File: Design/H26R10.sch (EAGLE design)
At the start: 66 parts, among them P1 HEXABIT_17.32_X2_NO_P5_P10_P1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, U1 STM32F091CBU6, U2 AD8275BRMZ, U3 ADR431ARMZ, U4 AD8295BCPZ-WP, U5 AD7687BRMZ, X1 XTALL_CSTCE8M00G52, X2 1751251, X3 CON-PHOENIX-350_1751277

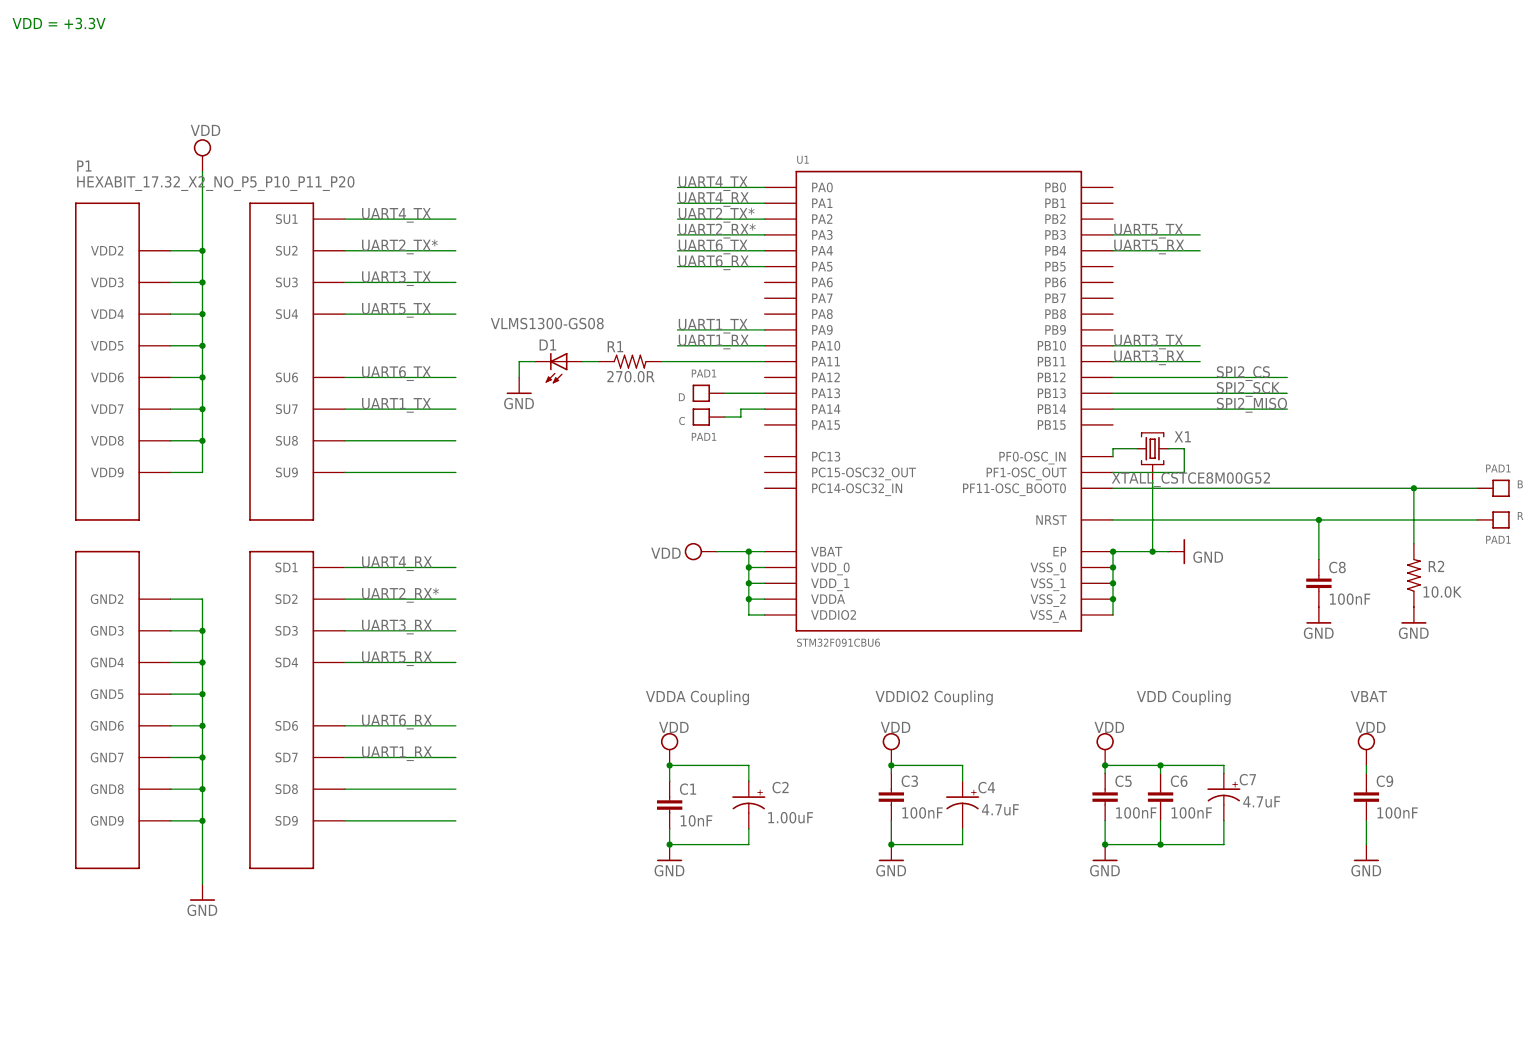
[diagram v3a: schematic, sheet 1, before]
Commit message: Replace MCU with Add STM32F091RB (LQFP64) and connect UARTs
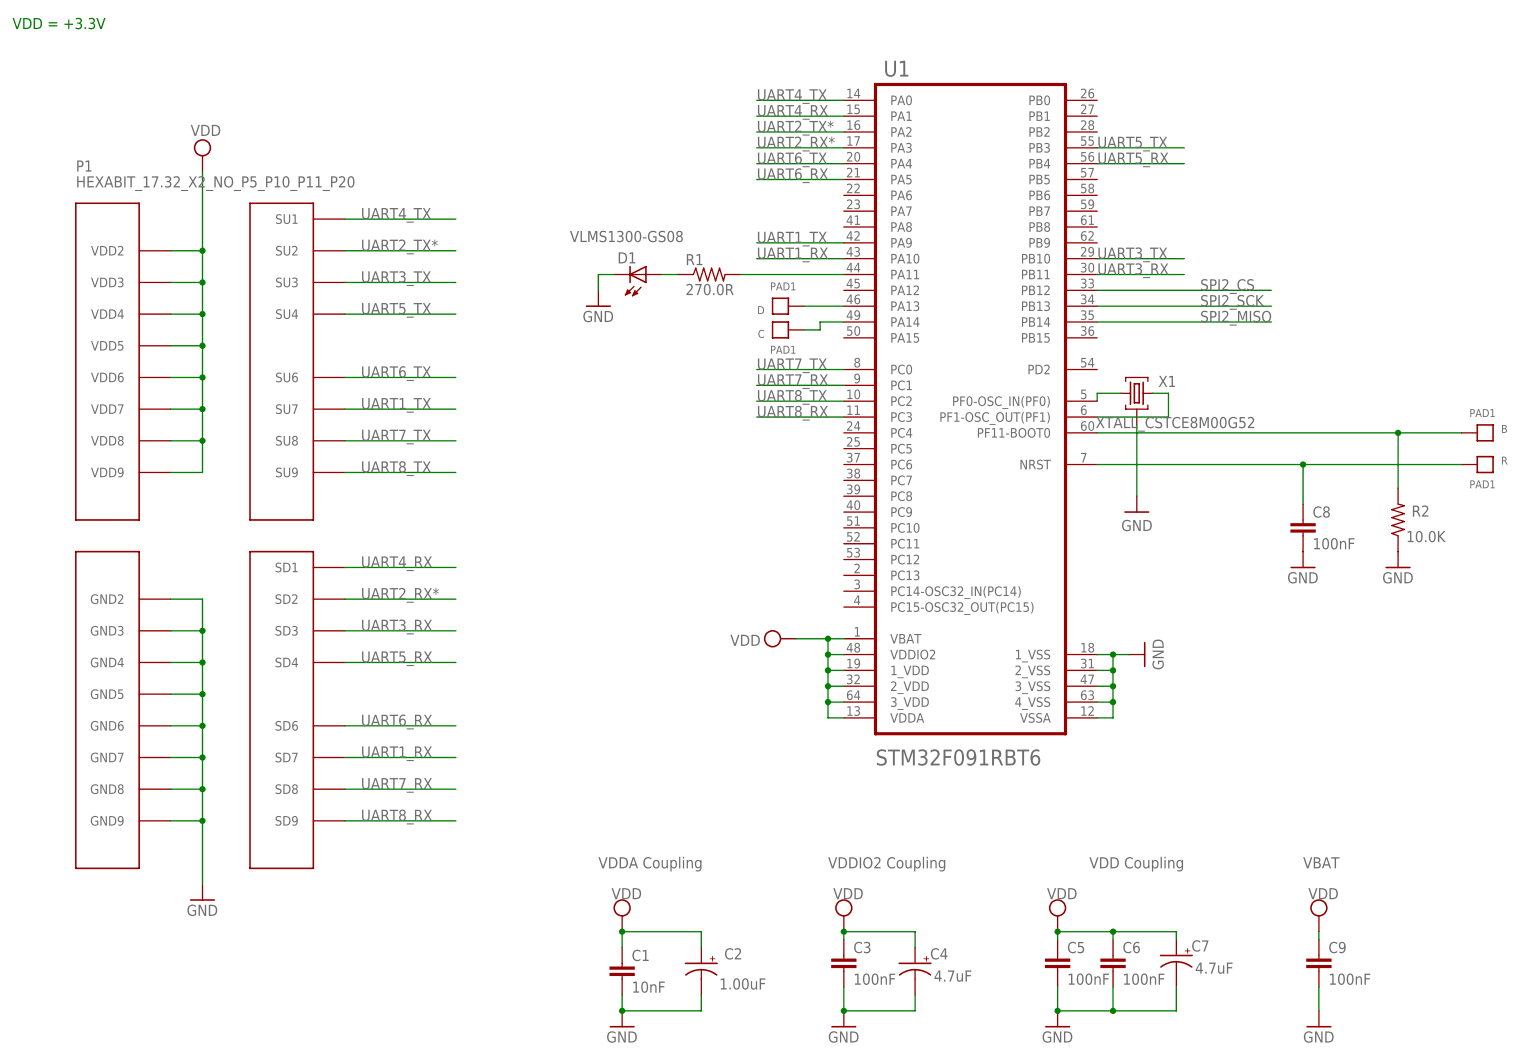
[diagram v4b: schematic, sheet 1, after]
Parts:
- U1: value STM32F091CBU6 -> STM32F091RBT6STMICROELECTRONICS_STM32F091RBT6_0_1; device Hexabitz:STM32F091CBU6 -> Hexabitz:STM32F091RBT6STMICROELECTRONICS_STM32F091RBT6_0_1
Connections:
- new net UART7_RX: U1.PC1
- new net UART7_TX: U1.PC0
- new net UART8_RX: U1.PC3
- new net UART8_TX: U1.PC2
- net B1: now also U1.PF11-BOOT0; no longer U1.PF11-OSC_BOOT0
- net GND: now also U1.1_VSS, U1.2_VSS, U1.3_VSS, U1.4_VSS, U1.VSSA; no longer U1.EP, U1.VSS_0, U1.VSS_1, U1.VSS_2, U1.VSS_A
- net N$5: now also U1.PF0-OSC_IN(PF0); no longer U1.PF0-OSC_IN
- net N$6: now also U1.PF1-OSC_OUT(PF1); no longer U1.PF1-OSC_OUT
- net VDD: now also U1.1_VDD, U1.2_VDD, U1.3_VDD; no longer U1.VDD_0, U1.VDD_1
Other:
- moved on the sheet: B, C, C1, C2, C3, C4, C5, C6, C7, C8, C9, D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

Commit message: Rearrange uart connections Route analog section
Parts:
- R3, R4, R6, R7, R8: device Hexabitz:R-0805 -> Hexabitz:R-0603
- renumbered X2 to PWR, X3 to AIN
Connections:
- net +5V renamed +2.5V
- removed net N$29: P1.SU1
- removed net N$30: P1.SU2
- removed net N$34: P1.SD1, P1.SD2, P1.SD3, P1.SD4, P1.SD6, P1.SD7, P1.SD8, P1.SD9, P1.SU3, P1.SU4, P1.SU6, P1.SU7, P1.SU8, P1.SU9
- removed net UART1_RX: U1.PA10
- removed net UART1_TX: U1.PA9
- new net UART1_RX*: P1.SD7, U1.PA10
- new net UART1_TX*: P1.SU7, U1.PA9
- net UART2_RX*: now also P1.SD3
- net UART2_TX*: now also P1.SU3
- net UART3_RX: now also P1.SD6
- net UART3_TX: now also P1.SU6
- net UART4_RX: now also P1.SD2
- net UART4_TX: now also P1.SU2
- net UART5_RX: now also P1.SD8
- net UART5_TX: now also P1.SU8
- net UART6_RX: now also P1.SD4
- net UART6_TX: now also P1.SU4
- net UART7_RX: now also P1.SD9
- net UART7_TX: now also P1.SU9
- net UART8_RX: now also P1.SD1
- net UART8_TX: now also P1.SU1

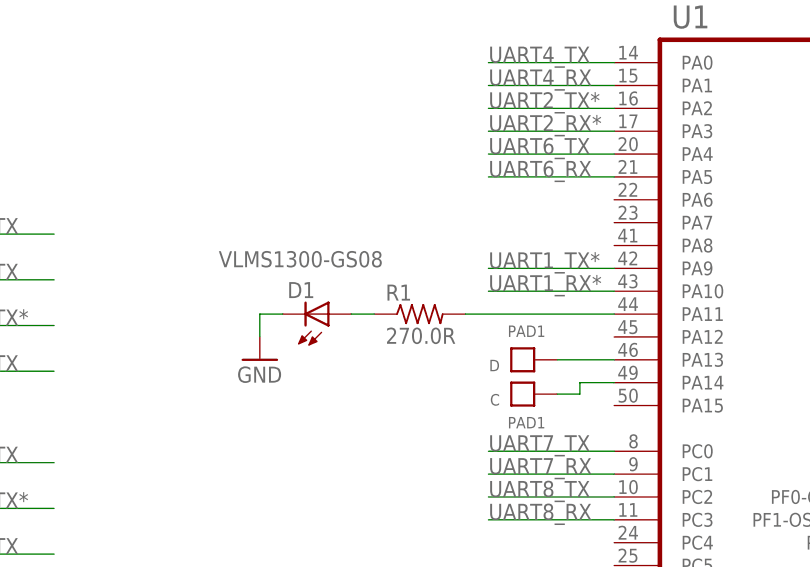
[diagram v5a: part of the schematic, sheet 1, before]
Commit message: More routing Add 2 more layers Add layer stack note
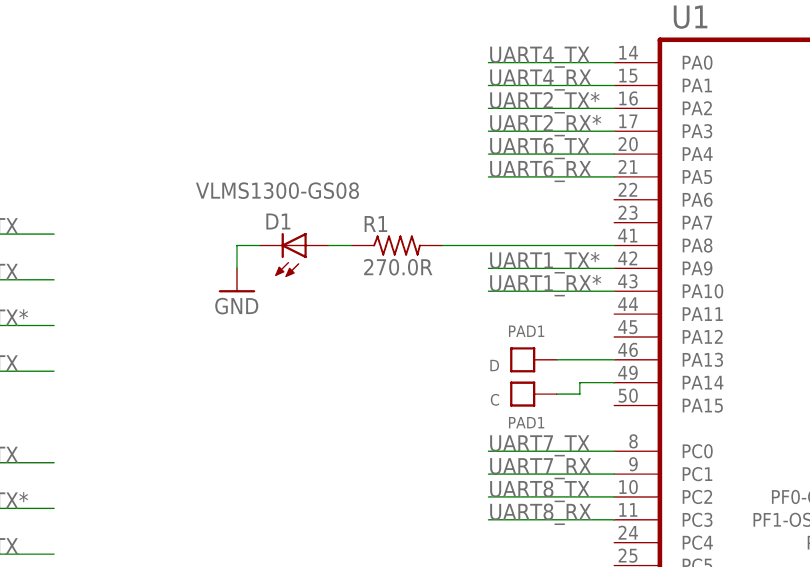
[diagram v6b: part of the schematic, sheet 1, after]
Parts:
- R5: device Hexabitz:R-0805 -> Hexabitz:R-0603
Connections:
- net N$3: now also U1.PA8; no longer U1.PA11
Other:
- moved on the sheet: D1, R1
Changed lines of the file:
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@@
 <setting verticaltext="up"/>
 </settings>
-<grid distance="50" unitdist="mil" unit="mil" style="lines" multiple="1" display="no" altdistance="0.01" altunitdist="inch" altunit="inch"/>
+<grid distance="0.1" unitdist="inch" unit="inch" style="lines" multiple="1" display="no" altdistance="0.01" altunitdist="inch" altunit="inch"/>
 <layers>
 <layer number="1" name="Top" color="4" fill="1" visible="no" active="no"/>
@@
 <part name="SUPPLY3" library="supply2" deviceset="VDD" device=""/>
 <part name="SUPPLY16" library="supply2" library_urn="urn:adsk.eagle:library:372" deviceset="+5V" device="" value="A2V5"/>
-<part name="R5" library="Hexabitz" deviceset="R-0805" device="" value="1.00K">
+<part name="R5" library="Hexabitz" deviceset="R-0603" device="" value="1.00K">
 <attribute name="MFN" value="Yageo"/>
 <attribute name="MPN" value="RC0603FR-0710KL"/>
@@
 <attribute name="VALUE" x="136.144" y="49.149" size="1.778" layer="96" rot="MR0"/>
 </instance>
-<instance part="R1" gate="G$1" x="127" y="163.83" smashed="yes">
-<attribute name="NAME" x="123.19" y="165.3286" size="1.778" layer="95"/>
-<attribute name="VALUE" x="123.19" y="160.528" size="1.778" layer="96"/>
-</instance>
-<instance part="D1" gate="G$1" x="116.84" y="163.83" smashed="yes" rot="MR180">
-<attribute name="NAME" x="112.268" y="167.386" size="1.778" layer="95" rot="MR180"/>
-<attribute name="VALUE" x="104.648" y="170.815" size="1.778" layer="96" rot="MR180"/>
+<instance part="R1" gate="G$1" x="124.46" y="171.45" smashed="yes">
+<attribute name="NAME" x="120.65" y="172.9486" size="1.778" layer="95"/>
+<attribute name="VALUE" x="120.65" y="168.148" size="1.778" layer="96"/>
+</instance>
+<instance part="D1" gate="G$1" x="114.3" y="171.45" smashed="yes" rot="MR180">
+<attribute name="NAME" x="109.728" y="175.006" size="1.778" layer="95" rot="MR180"/>
+<attribute name="VALUE" x="102.108" y="178.435" size="1.778" layer="96" rot="MR180"/>
 </instance>
 <instance part="X1" gate="G$1" x="195.58" y="144.78" smashed="yes">
@@
 <attribute name="VALUE" x="214.63" y="140.97" size="1.778" layer="96" rot="R180"/>
 </instance>
-<instance part="GND1" gate="1" x="109.22" y="158.75" smashed="yes">
-<attribute name="VALUE" x="106.68" y="156.21" size="1.778" layer="96"/>
+<instance part="GND1" gate="1" x="106.68" y="166.37" smashed="yes">
+<attribute name="VALUE" x="104.14" y="163.83" size="1.778" layer="96"/>
 </instance>
 <instance part="SUPPLY4" gate="G$1" x="138.43" y="105.41" smashed="yes" rot="R90">
@@
 <segment>
 <pinref part="GND1" gate="1" pin="GND"/>
-<wire x1="109.22" y1="161.29" x2="109.22" y2="163.83" width="0.1524" layer="91"/>
+<wire x1="106.68" y1="168.91" x2="106.68" y2="171.45" width="0.1524" layer="91"/>
 <pinref part="D1" gate="G$1" pin="C"/>
-<wire x1="109.22" y1="163.83" x2="111.76" y2="163.83" width="0.1524" layer="91"/>
+<wire x1="106.68" y1="171.45" x2="109.22" y2="171.45" width="0.1524" layer="91"/>
 </segment>
 <segment>
@@
 </segment>
 </net>
-<net name="N$3" class="0">
-<segment>
-<pinref part="R1" gate="G$1" pin="2"/>
-<wire x1="148.59" y1="163.83" x2="132.08" y2="163.83" width="0.1524" layer="91"/>
-<pinref part="U1" gate="G$0" pin="PA11"/>
-</segment>
-</net>
 <net name="N$4" class="0">
 <segment>
 <pinref part="R1" gate="G$1" pin="1"/>
 <pinref part="D1" gate="G$1" pin="A"/>
-<wire x1="121.92" y1="163.83" x2="119.38" y2="163.83" width="0.1524" layer="91"/>
+<wire x1="119.38" y1="171.45" x2="116.84" y2="171.45" width="0.1524" layer="91"/>
 </segment>
 </net>
@@
 </segment>
 </net>
+<net name="N$3" class="0">
+<segment>
+<pinref part="R1" gate="G$1" pin="2"/>
+<pinref part="U1" gate="G$0" pin="PA8"/>
+<wire x1="129.54" y1="171.45" x2="148.59" y2="171.45" width="0.1524" layer="91"/>
+</segment>
+</net>

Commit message: Finished routing Added polygons
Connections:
- removed net N$24: C13.2, C14.1, FB2.2
- net AGND: now also C11.GND, C12.GND, C13.2, C14.1, FB2.2
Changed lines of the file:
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@@
 <setting verticaltext="up"/>
 </settings>
-<grid distance="0.1" unitdist="inch" unit="inch" style="lines" multiple="1" display="no" altdistance="0.01" altunitdist="inch" altunit="inch"/>
+<grid distance="50" unitdist="mil" unit="mil" style="lines" multiple="1" display="no" altdistance="0.01" altunitdist="inch" altunit="inch"/>
 <layers>
 <layer number="1" name="Top" color="4" fill="1" visible="no" active="no"/>
@@
 </part>
 <part name="SUPPLY22" library="supply2" library_urn="urn:adsk.eagle:library:372" deviceset="AGND" device=""/>
-<part name="SUPPLY19" library="supply2" library_urn="urn:adsk.eagle:library:372" deviceset="AGND" device=""/>
 <part name="SUPPLY28" library="supply2" library_urn="urn:adsk.eagle:library:372" deviceset="AGND" device=""/>
 <part name="SUPPLY27" library="supply2" library_urn="urn:adsk.eagle:library:372" deviceset="+5V" device="" value="A2V5"/>
@@
 <attribute name="VALUE" x="157.353" y="32.385" size="1.778" layer="96"/>
 </instance>
-<instance part="SUPPLY19" gate="G$1" x="149.86" y="35.56" smashed="yes">
-<attribute name="VALUE" x="147.193" y="32.385" size="1.778" layer="96"/>
-</instance>
 <instance part="SUPPLY28" gate="G$1" x="210.82" y="35.56" smashed="yes">
 <attribute name="VALUE" x="208.153" y="32.385" size="1.778" layer="96"/>
@@
 </segment>
 <segment>
+<pinref part="C18" gate="G$1" pin="2"/>
+<pinref part="FB2" gate="G$1" pin="2"/>
+<wire x1="149.86" y1="39.37" x2="149.86" y2="41.91" width="0.1524" layer="91"/>
+<wire x1="109.22" y1="39.37" x2="121.92" y2="39.37" width="0.1524" layer="91"/>
+<pinref part="C13" gate="G$1" pin="2"/>
+<wire x1="121.92" y1="39.37" x2="138.43" y2="39.37" width="0.1524" layer="91"/>
+<wire x1="138.43" y1="41.91" x2="138.43" y2="39.37" width="0.1524" layer="91"/>
+<junction x="138.43" y="39.37"/>
+<pinref part="C14" gate="G$1" pin="1"/>
+<wire x1="138.43" y1="39.37" x2="138.43" y2="36.83" width="0.1524" layer="91"/>
+<pinref part="C11" gate="G$0" pin="GND"/>
+<wire x1="121.92" y1="43.18" x2="121.92" y2="39.37" width="0.1524" layer="91"/>
+<junction x="121.92" y="39.37"/>
+<pinref part="C12" gate="G$0" pin="GND"/>
+<wire x1="121.92" y1="39.37" x2="121.92" y2="35.56" width="0.1524" layer="91"/>
+<wire x1="138.43" y1="39.37" x2="149.86" y2="39.37" width="0.1524" layer="91"/>
+<junction x="149.86" y="39.37"/>
 <pinref part="C19" gate="G$1" pin="2"/>
 <pinref part="SUPPLY22" gate="G$1" pin="AGND"/>
-<wire x1="160.02" y1="38.1" x2="160.02" y2="41.91" width="0.1524" layer="91"/>
-</segment>
-<segment>
-<pinref part="C18" gate="G$1" pin="2"/>
-<pinref part="SUPPLY19" gate="G$1" pin="AGND"/>
-<wire x1="149.86" y1="38.1" x2="149.86" y2="41.91" width="0.1524" layer="91"/>
+<wire x1="160.02" y1="38.1" x2="160.02" y2="39.37" width="0.1524" layer="91"/>
+<wire x1="160.02" y1="39.37" x2="160.02" y2="41.91" width="0.1524" layer="91"/>
+<wire x1="149.86" y1="39.37" x2="160.02" y2="39.37" width="0.1524" layer="91"/>
+<junction x="160.02" y="39.37"/>
 </segment>
 <segment>
@@
 </segment>
 </net>
-<net name="N$24" class="0">
-<segment>
-<pinref part="FB2" gate="G$1" pin="2"/>
-<wire x1="109.22" y1="39.37" x2="121.92" y2="39.37" width="0.1524" layer="91"/>
-<wire x1="121.92" y1="39.37" x2="138.43" y2="39.37" width="0.1524" layer="91"/>
-<wire x1="121.92" y1="45.72" x2="121.92" y2="39.37" width="0.1524" layer="91"/>
-<junction x="121.92" y="39.37"/>
-<wire x1="121.92" y1="33.02" x2="121.92" y2="39.37" width="0.1524" layer="91"/>
-<pinref part="C13" gate="G$1" pin="2"/>
-<wire x1="138.43" y1="41.91" x2="138.43" y2="39.37" width="0.1524" layer="91"/>
-<junction x="138.43" y="39.37"/>
-<pinref part="C14" gate="G$1" pin="1"/>
-<wire x1="138.43" y1="39.37" x2="138.43" y2="36.83" width="0.1524" layer="91"/>
-</segment>
-</net>

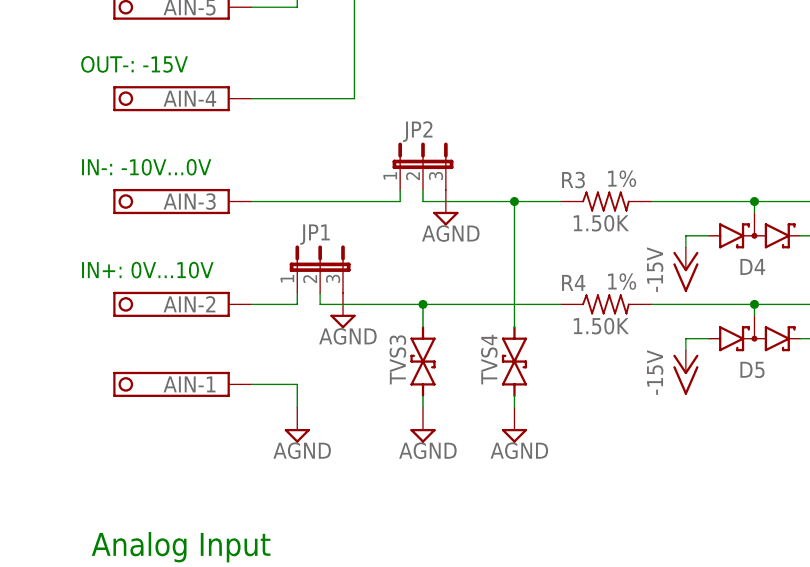
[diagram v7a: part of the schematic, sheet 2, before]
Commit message: Finished routing and silkscreen.. Reviewed ERC and DRC PCB is done
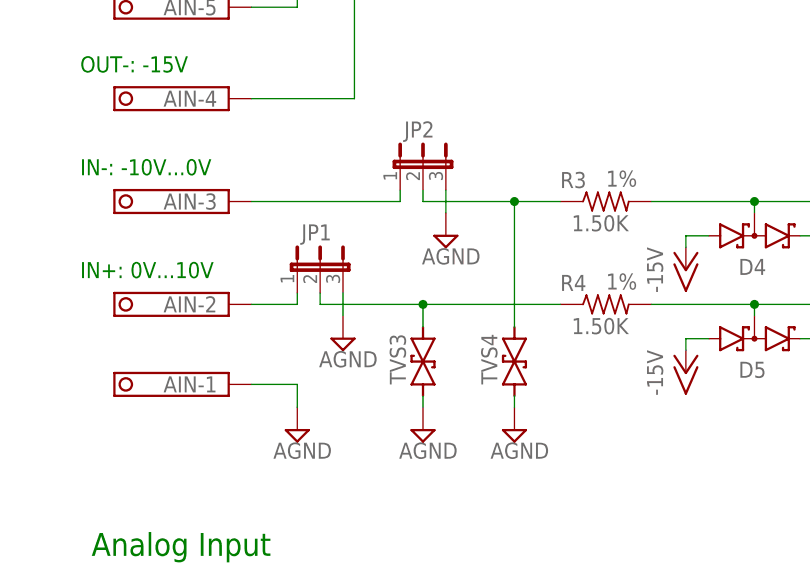
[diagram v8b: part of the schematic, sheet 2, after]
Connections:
- net GND: now also U1.PA11, U1.PA12
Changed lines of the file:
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@@
 <part name="U1" library="Hexabitz" deviceset="STM32F091RBT6" device="STMICROELECTRONICS_STM32F091RBT6_0_1"/>
 <part name="GND11" library="supply1" deviceset="GND" device=""/>
+<part name="GND12" library="supply1" deviceset="GND" device=""/>
 </parts>
 <sheets>
@@
 <attribute name="VALUE" x="198.12" y="105.41" size="1.778" layer="96" rot="R270"/>
 </instance>
+<instance part="GND12" gate="1" x="130.81" y="163.83" smashed="yes" rot="R270">
+<attribute name="VALUE" x="128.27" y="166.37" size="1.778" layer="96" rot="R270"/>
+</instance>
 </instances>
 <busses>
@@
 <junction x="191.77" y="95.25"/>
 </segment>
+<segment>
+<pinref part="GND12" gate="1" pin="GND"/>
+<pinref part="U1" gate="G$0" pin="PA11"/>
+<wire x1="133.35" y1="163.83" x2="147.32" y2="163.83" width="0.1524" layer="91"/>
+<pinref part="U1" gate="G$0" pin="PA12"/>
+<wire x1="147.32" y1="163.83" x2="148.59" y2="163.83" width="0.1524" layer="91"/>
+<wire x1="148.59" y1="161.29" x2="147.32" y2="161.29" width="0.1524" layer="91"/>
+<wire x1="147.32" y1="161.29" x2="147.32" y2="163.83" width="0.1524" layer="91"/>
+<junction x="147.32" y="163.83"/>
+</segment>
 </net>
 <net name="UART5_TX" class="0">
@@
 <attribute name="VALUE" x="255.143" y="32.385" size="1.778" layer="96"/>
 </instance>
-<instance part="SUPPLY13" gate="G$1" x="91.44" y="166.37" smashed="yes">
-<attribute name="VALUE" x="88.773" y="163.195" size="1.778" layer="96"/>
+<instance part="SUPPLY13" gate="G$1" x="91.44" y="163.83" smashed="yes">
+<attribute name="VALUE" x="88.773" y="160.655" size="1.778" layer="96"/>
 </instance>
-<instance part="SUPPLY11" gate="G$1" x="80.01" y="154.94" smashed="yes">
-<attribute name="VALUE" x="77.343" y="151.765" size="1.778" layer="96"/>
+<instance part="SUPPLY11" gate="G$1" x="80.01" y="152.4" smashed="yes">
+<attribute name="VALUE" x="77.343" y="149.225" size="1.778" layer="96"/>
 </instance>
 <instance part="P+3" gate="1" x="74.93" y="195.58" smashed="yes">
@@
 <pinref part="JP2" gate="1" pin="3"/>
 <pinref part="SUPPLY13" gate="G$1" pin="AGND"/>
+<wire x1="91.44" y1="166.37" x2="91.44" y2="168.91" width="0.1524" layer="91"/>
 </segment>
 <segment>
@@
 <pinref part="SUPPLY11" gate="G$1" pin="AGND"/>
 <pinref part="JP1" gate="1" pin="3"/>
+<wire x1="80.01" y1="154.94" x2="80.01" y2="157.48" width="0.1524" layer="91"/>
 </segment>
 <segment>
@@
 </sheet>
 </sheets>
+<errors>
+</errors>
 </schematic>
 </drawing>
